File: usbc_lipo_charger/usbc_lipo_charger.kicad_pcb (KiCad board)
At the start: 2 copper layers, 39 x 15.5 mm, 18 parts, among them J1 USB_C_Receptacle_PowerOnly_6P, J2 Conn_01x02, U1 MCP73833-xxx-UN

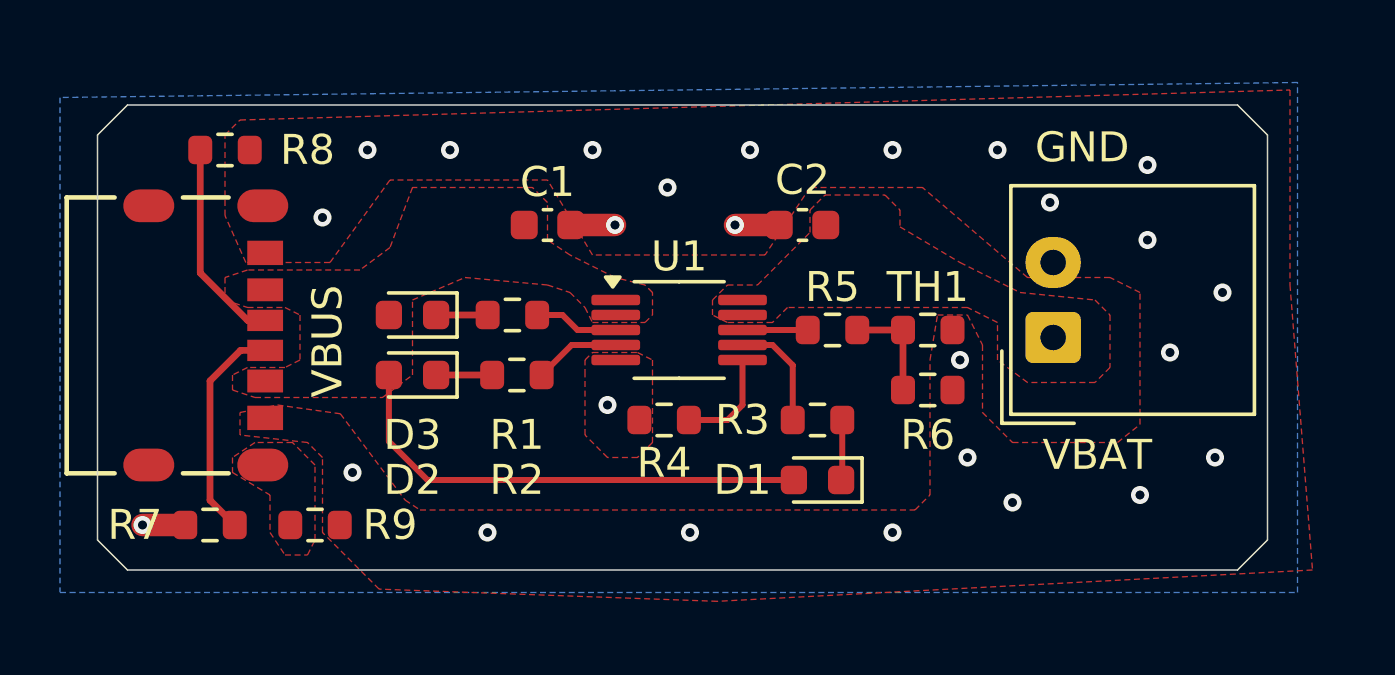
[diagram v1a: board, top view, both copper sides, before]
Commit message: revision 1, make smaller, add pcb heatsinking, label status leds
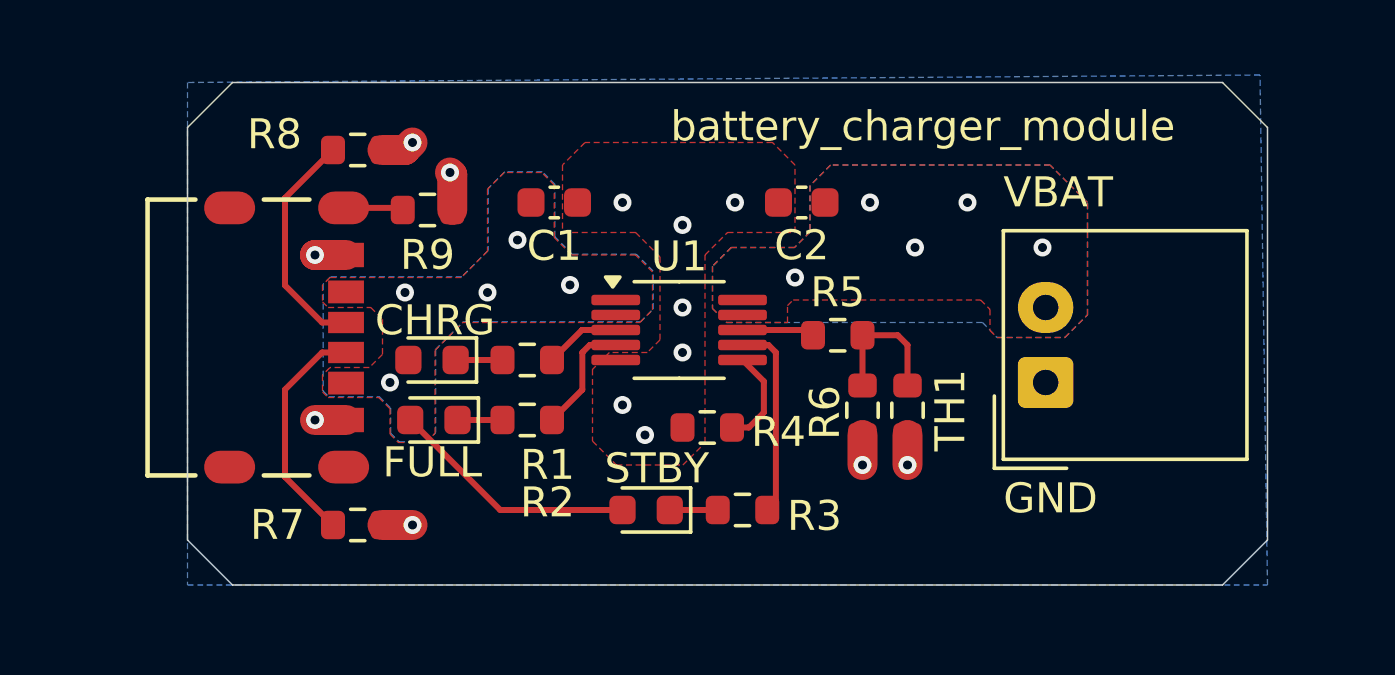
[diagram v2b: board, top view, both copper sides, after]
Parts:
- moved R9 11.1 mm to (140.5, 75.0)
- moved D1 5.80 mm to (147.8, 85.0)
- moved R7 4.93 mm to (138.2, 85.5), turned to 0 degrees
- moved R8 4.43 mm to (138.2, 73.0)
- moved R3 3.91 mm to (151.0, 85.0), turned to 0 degrees
- moved TH1 2.76 mm to (156.5, 81.7), turned to -90 degrees
- moved J1 2.70 mm to (134.8, 79.2)
- moved R6 2.28 mm to (155.0, 81.7), turned to -90 degrees
- moved D2 1.66 mm to (140.7, 82.0)
- moved D3 1.63 mm to (140.7, 80.0)
- moved R1 1.58 mm to (143.8, 80.0)
- moved R2 1.54 mm to (143.8, 82.0)
- moved J2 1.52 mm to (161.1, 80.8)
- moved R4 1.46 mm to (149.8, 82.2)
- moved C1 0.78 mm to (144.7, 74.8)
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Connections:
- J1 pad 7: (no net) -> Net-(J1-SHIELD)
- J1 pad 8: Net-(J1-SHIELD) -> (no net)
- J2 pad 1: /VBAT -> GND
- J2 pad 2: GND -> /VBAT
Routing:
- net /VBUS: track 16.2 -> 8.32 mm, vias 0 -> 5
- net GND: track 4.38 -> 7.45 mm, vias 26 -> 14
- net Net-(U1-~{PG}): track 3.78 -> 6.59 mm
- net Net-(J1-SHIELD): track 0.00 -> 2.00 mm
- net /THERM: track 3.53 -> 4.66 mm
- net Net-(U1-STAT2): track 2.88 -> 3.89 mm
- net /CC1: track 6.92 -> 7.72 mm
- net /VBAT: vias 0 -> 5
- added copper zone on B.Cu, net /VBAT
- added copper zone on B.Cu, net /VBUS
- removed copper zone on F.Cu, net Net-(J1-SHIELD)
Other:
- board size 39 x 15.5 mm -> 36 x 16.8 mm
- board text added: "CHRG"
- board text added: "FULL"
- board text added: "STBY"
- board text added: "battery_charger_module"
- board text added: "daniel monahan '25"
- board text added: "rev1"
- board text removed: "1 cell Li battery charging module"
- board text removed: "VBUS"
- board text removed: "daniel monahan 2025"
- board text removed: "rev.1"

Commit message: add groundplane on front copper of pcb
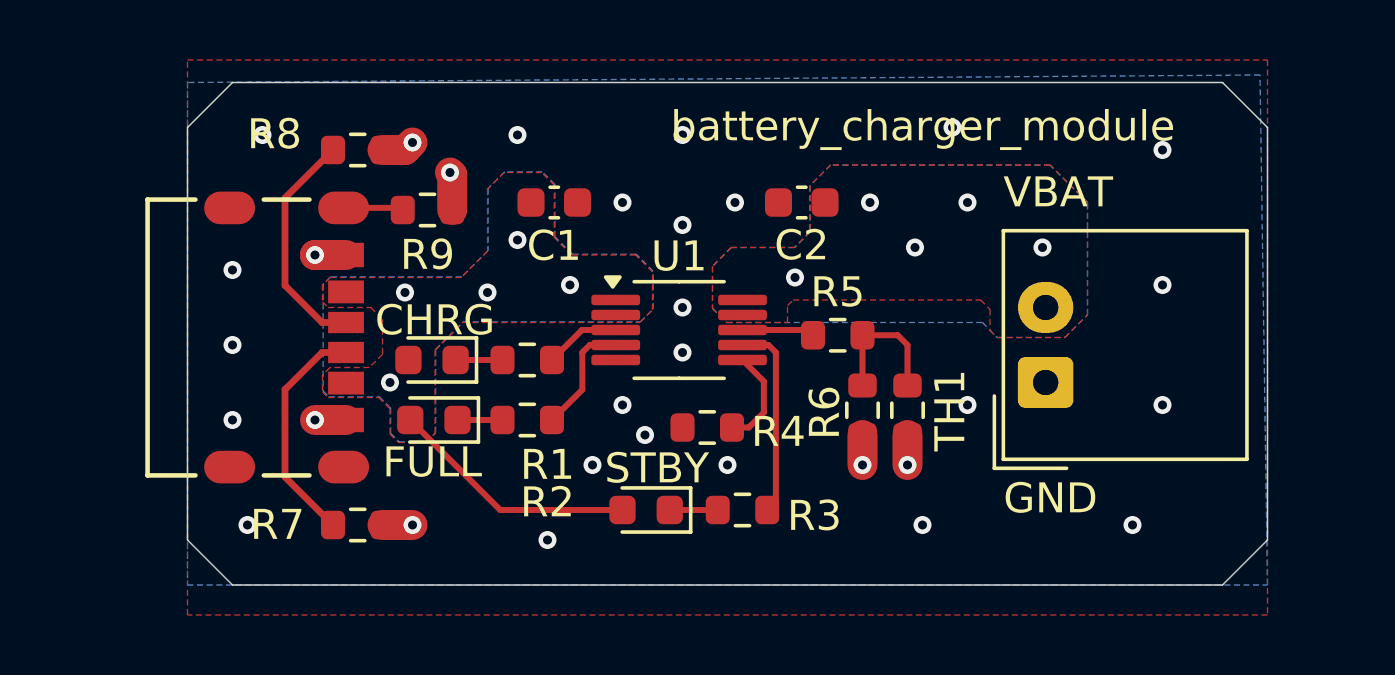
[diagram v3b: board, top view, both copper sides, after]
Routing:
- net GND: vias 14 -> 31
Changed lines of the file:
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@@
+	)
+	(via
+		(at 158.5 81.5)
+		(size 0.6)
+		(drill 0.3)
+		(layers "F.Cu" "B.Cu")
+		(free yes)
+		(net 1)
+	)
+	(via
+		(at 134.5 85.5)
+		(size 0.6)
+		(drill 0.3)
+		(layers "F.Cu" "B.Cu")
+		(free yes)
+		(net 1)
 	)
 	(via
@@
 	)
 	(via
+		(at 135 72.5)
+		(size 0.6)
+		(drill 0.3)
+		(layers "F.Cu" "B.Cu")
+		(free yes)
+		(net 1)
+	)
+	(via
+		(at 164 85.5)
+		(size 0.6)
+		(drill 0.3)
+		(layers "F.Cu" "B.Cu")
+		(free yes)
+		(net 1)
+	)
+	(via
+		(at 150.5 83.5)
+		(size 0.6)
+		(drill 0.3)
+		(layers "F.Cu" "B.Cu")
+		(free yes)
+		(net 1)
+	)
+	(via
+		(at 134 79.5)
+		(size 0.6)
+		(drill 0.3)
+		(layers "F.Cu" "B.Cu")
+		(free yes)
+		(net 1)
+	)
+	(via
+		(at 143.5 72.5)
+		(size 0.6)
+		(drill 0.3)
+		(layers "F.Cu" "B.Cu")
+		(free yes)
+		(net 1)
+	)
+	(via
+		(at 149 72.5)
+		(size 0.6)
+		(drill 0.3)
+		(layers "F.Cu" "B.Cu")
+		(free yes)
+		(net 1)
+	)
+	(via
 		(at 136.75 76.5)
 		(size 0.6)
@@
 	)
 	(via
+		(at 134 77)
+		(size 0.6)
+		(drill 0.3)
+		(layers "F.Cu" "B.Cu")
+		(free yes)
+		(net 1)
+	)
+	(via
 		(at 147 74.75)
 		(size 0.6)
@@
 	)
 	(via
+		(at 144.5 86)
+		(size 0.6)
+		(drill 0.3)
+		(layers "F.Cu" "B.Cu")
+		(free yes)
+		(net 1)
+	)
+	(via
 		(at 141.25 73.75)
 		(size 0.6)
@@
 	)
 	(via
+		(at 157 85.5)
+		(size 0.6)
+		(drill 0.3)
+		(layers "F.Cu" "B.Cu")
+		(free yes)
+		(net 1)
+	)
+	(via
 		(at 140 72.75)
 		(size 0.6)
@@
 	)
 	(via
+		(at 146 83.5)
+		(size 0.6)
+		(drill 0.3)
+		(layers "F.Cu" "B.Cu")
+		(free yes)
+		(net 1)
+	)
+	(via
 		(at 149 79.75)
 		(size 0.6)
@@
 	)
 	(via
+		(at 165 81.5)
+		(size 0.6)
+		(drill 0.3)
+		(layers "F.Cu" "B.Cu")
+		(free yes)
+		(net 1)
+	)
+	(via
+		(at 165 73)
+		(size 0.6)
+		(drill 0.3)
+		(layers "F.Cu" "B.Cu")
+		(free yes)
+		(net 1)
+	)
+	(via
+		(at 165 77.5)
+		(size 0.6)
+		(drill 0.3)
+		(layers "F.Cu" "B.Cu")
+		(free yes)
+		(net 1)
+	)
+	(via
 		(at 155 83.5)
 		(size 0.6)
@@
 	)
 	(via
+		(at 134 82)
+		(size 0.6)
+		(drill 0.3)
+		(layers "F.Cu" "B.Cu")
+		(free yes)
+		(net 1)
+	)
+	(via
 		(at 140 85.5)
 		(size 0.6)
@@
 	(via
 		(at 147.75 82.5)
+		(size 0.6)
+		(drill 0.3)
+		(layers "F.Cu" "B.Cu")
+		(free yes)
+		(net 1)
+	)
+	(via
+		(at 158 72.25)
 		(size 0.6)
 		(drill 0.3)
@@
 		(start 135.75 74.6)
 		(end 137.35 73)
-		(width 0.2)
+		(width 0.225)
 		(layer "F.Cu")
 		(net 6)
@@
 		(start 137.784401 78.750001)
 		(end 136.987501 78.750001)
-		(width 0.2)
+		(width 0.225)
 		(layer "F.Cu")
 		(net 6)
@@
 		(start 135.75 77.5125)
 		(end 135.75 74.6)
-		(width 0.2)
+		(width 0.225)
 		(layer "F.Cu")
 		(net 6)
@@
 		(start 136.987501 78.750001)
 		(end 135.75 77.5125)
-		(width 0.2)
+		(width 0.225)
 		(layer "F.Cu")
 		(net 6)
@@
 		(start 135.75 83.9)
 		(end 137.35 85.5)
-		(width 0.2)
+		(width 0.225)
 		(layer "F.Cu")
 		(net 8)
@@
 		(start 135.75 80.9875)
 		(end 135.75 83.9)
-		(width 0.2)
+		(width 0.225)
 		(layer "F.Cu")
 		(net 8)
@@
 		(start 136.987501 79.749999)
 		(end 135.75 80.9875)
-		(width 0.2)
+		(width 0.225)
 		(layer "F.Cu")
 		(net 8)
@@
 		(start 137.784401 79.749999)
 		(end 136.987501 79.749999)
-		(width 0.2)
+		(width 0.225)
 		(layer "F.Cu")
 		(net 8)
@@
 		(layer "F.Cu")
 		(hatch edge 0.5)
-		(priority 2)
-		(connect_pads yes
+		(connect_pads
 			(clearance 0.3)
 		)
@@
 		(polygon
 			(pts
-				(xy 145 75.75) (xy 147.4375 75.75) (xy 148.25 76.5625) (xy 148.25 79.328125) (xy 147.828125 79.75)
-				(xy 146.5625 79.75) (xy 146 80.3125) (xy 146 82.703125) (xy 146.796875 83.5) (xy 149.011719 83.5)
-				(xy 149.75 82.761719) (xy 149.75 76.5) (xy 150.5 75.75) (xy 152.75 75.75) (xy 152.75 73.5) (xy 152 72.75)
-				(xy 145.75 72.75) (xy 145 73.5)
+				(xy 132.5 70) (xy 168.5 70) (xy 168.5 88.5) (xy 132.5 88.5)
 			)
 		)

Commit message: update pcb image, meet manufacture requirements
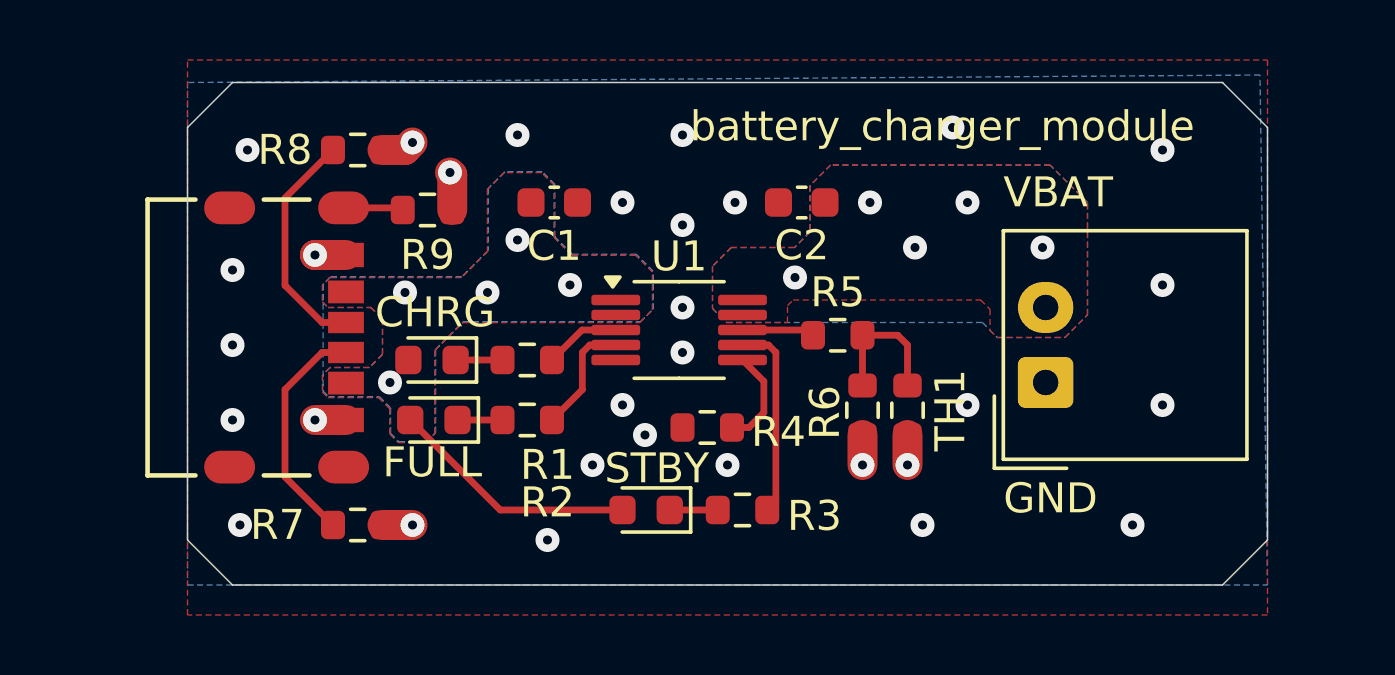
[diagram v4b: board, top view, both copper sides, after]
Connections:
- net /VBUS renamed Net-(D1-A)
